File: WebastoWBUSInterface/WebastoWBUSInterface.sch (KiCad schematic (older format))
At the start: 14 parts, among them J1 FTDI Interface, J2 WBUS, Q1 BC548, Q2 BC548, Q3 BC548, Q4 BC557

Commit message: Larger resistor hole sizes
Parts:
- J2: footprint Socket_Strips:Socket_Strip_Angled_1x03_Pitch2.54mm -> Connectors_Terminal_Blocks:TerminalBlock_bornier-3_P5.08mm
- R1, R10, R3, R5, R7, R8, R9: footprint Resistors_THT:R_Axial_DIN0204_L3.6mm_D1.6mm_P5.08mm_Horizontal -> Resistors_THT:R_Axial_DIN0207_L6.3mm_D2.5mm_P7.62mm_Horizontal
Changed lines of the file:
@@
 EESchema Schematic File Version 4
+LIBS:WebastoWBUSInterface-cache
 EELAYER 29 0
 EELAYER END
@@
 F 1 "BC548" H 2400 3540 50  0000 L CNN
 F 2 "TO_SOT_Packages_THT:TO-92_Molded_Narrow" H 2780 3305 50  0001 L CIN
-F 3 "http://www.fairchildsemi.com/ds/BC/BC547.pdf" H 2580 3380 50  0001 L CNN
+F 3 "https://en.wikipedia.org/wiki/BC548" H 2580 3380 50  0001 L CNN
 	1    2580 3380
 	1    0    0    -1
@@
 F 0 "R7" H 3260 3256 50  0000 L CNN
 F 1 "10K" H 3260 3165 50  0000 L CNN
-F 2 "Resistors_THT:R_Axial_DIN0204_L3.6mm_D1.6mm_P5.08mm_Horizontal" V 3120 3210 50  0001 C CNN
+F 2 "Resistors_THT:R_Axial_DIN0207_L6.3mm_D2.5mm_P7.62mm_Horizontal" V 3120 3210 50  0001 C CNN
 F 3 "~" H 3190 3210 50  0001 C CNN
 	1    3190 3210
@@
 F 1 "BC557" H 4461 3115 50  0000 L CNN
 F 2 "TO_SOT_Packages_THT:TO-92_Molded_Narrow" H 4470 2995 50  0001 L CIN
-F 3 "http://www.fairchildsemi.com/ds/BC/BC557.pdf" H 4270 3070 50  0001 L CNN
+F 3 "http://www.farnell.com/datasheets/296678.pdf" H 4270 3070 50  0001 L CNN
 	1    4270 3070
 	-1   0    0    1
@@
 F 0 "R9" H 3570 3186 50  0000 L CNN
 F 1 "1K" H 3570 3095 50  0000 L CNN
-F 2 "Resistors_THT:R_Axial_DIN0204_L3.6mm_D1.6mm_P5.08mm_Horizontal" V 3430 3140 50  0001 C CNN
+F 2 "Resistors_THT:R_Axial_DIN0207_L6.3mm_D2.5mm_P7.62mm_Horizontal" V 3430 3140 50  0001 C CNN
 F 3 "~" H 3500 3140 50  0001 C CNN
 	1    3500 3140
@@
 F 0 "R5" H 3570 3616 50  0000 L CNN
 F 1 "1K" H 3570 3525 50  0000 L CNN
-F 2 "Resistors_THT:R_Axial_DIN0204_L3.6mm_D1.6mm_P5.08mm_Horizontal" V 3430 3570 50  0001 C CNN
+F 2 "Resistors_THT:R_Axial_DIN0207_L6.3mm_D2.5mm_P7.62mm_Horizontal" V 3430 3570 50  0001 C CNN
 F 3 "~" H 3500 3570 50  0001 C CNN
 	1    3500 3570
@@
 F 0 "J2" H 5788 3306 50  0000 L CNN
 F 1 "WBUS" H 5788 3215 50  0000 L CNN
-F 2 "Socket_Strips:Socket_Strip_Angled_1x03_Pitch2.54mm" H 5760 3280 50  0001 C CNN
+F 2 "Connectors_Terminal_Blocks:TerminalBlock_bornier-3_P5.08mm" H 5760 3280 50  0001 C CNN
 F 3 "~" H 5760 3280 50  0001 C CNN
 	1    5760 3280
@@
 F 0 "R10" V 4413 3380 50  0000 C CNN
 F 1 "10K" V 4504 3380 50  0000 C CNN
-F 2 "Resistors_THT:R_Axial_DIN0204_L3.6mm_D1.6mm_P5.08mm_Horizontal" V 4550 3380 50  0001 C CNN
+F 2 "Resistors_THT:R_Axial_DIN0207_L6.3mm_D2.5mm_P7.62mm_Horizontal" V 4550 3380 50  0001 C CNN
 F 3 "~" H 4620 3380 50  0001 C CNN
 	1    4620 3380
@@
 F 0 "R3" H 4840 3024 50  0000 R CNN
 F 1 "1K" H 4840 3115 50  0000 R CNN
-F 2 "Resistors_THT:R_Axial_DIN0204_L3.6mm_D1.6mm_P5.08mm_Horizontal" V 4840 3070 50  0001 C CNN
+F 2 "Resistors_THT:R_Axial_DIN0207_L6.3mm_D2.5mm_P7.62mm_Horizontal" V 4840 3070 50  0001 C CNN
 F 3 "~" H 4910 3070 50  0001 C CNN
 	1    4910 3070
@@
 F 0 "R8" H 3120 3844 50  0000 R CNN
 F 1 "10K" H 3120 3935 50  0000 R CNN
-F 2 "Resistors_THT:R_Axial_DIN0204_L3.6mm_D1.6mm_P5.08mm_Horizontal" V 3120 3890 50  0001 C CNN
+F 2 "Resistors_THT:R_Axial_DIN0207_L6.3mm_D2.5mm_P7.62mm_Horizontal" V 3120 3890 50  0001 C CNN
 F 3 "~" H 3190 3890 50  0001 C CNN
 	1    3190 3890
@@
 F 1 "BC548" H 4431 4655 50  0000 L CNN
 F 2 "TO_SOT_Packages_THT:TO-92_Molded_Narrow" H 4440 4625 50  0001 L CIN
-F 3 "http://www.fairchildsemi.com/ds/BC/BC547.pdf" H 4240 4700 50  0001 L CNN
+F 3 "https://en.wikipedia.org/wiki/BC548" H 4240 4700 50  0001 L CNN
 	1    4240 4700
 	1    0    0    -1
@@
 F 0 "R1" V 4473 4500 50  0000 C CNN
 F 1 "10K" V 4564 4500 50  0000 C CNN
-F 2 "Resistors_THT:R_Axial_DIN0204_L3.6mm_D1.6mm_P5.08mm_Horizontal" V 4610 4500 50  0001 C CNN
+F 2 "Resistors_THT:R_Axial_DIN0207_L6.3mm_D2.5mm_P7.62mm_Horizontal" V 4610 4500 50  0001 C CNN
 F 3 "~" H 4680 4500 50  0001 C CNN
 	1    4680 4500
@@
 F 1 "BC548" H 5281 4455 50  0000 L CNN
 F 2 "TO_SOT_Packages_THT:TO-92_Molded_Narrow" H 5290 4425 50  0001 L CIN
-F 3 "http://www.fairchildsemi.com/ds/BC/BC547.pdf" H 5090 4500 50  0001 L CNN
+F 3 "https://en.wikipedia.org/wiki/BC548" H 5090 4500 50  0001 L CNN
 	1    5090 4500
 	1    0    0    -1

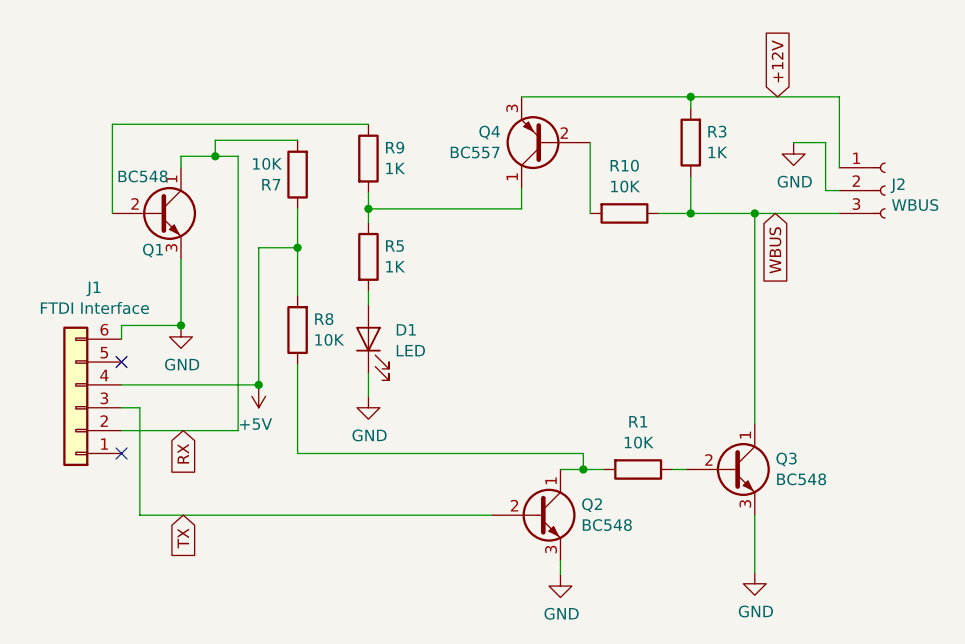
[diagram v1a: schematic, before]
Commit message: JLCPCB SMD board for full assembly
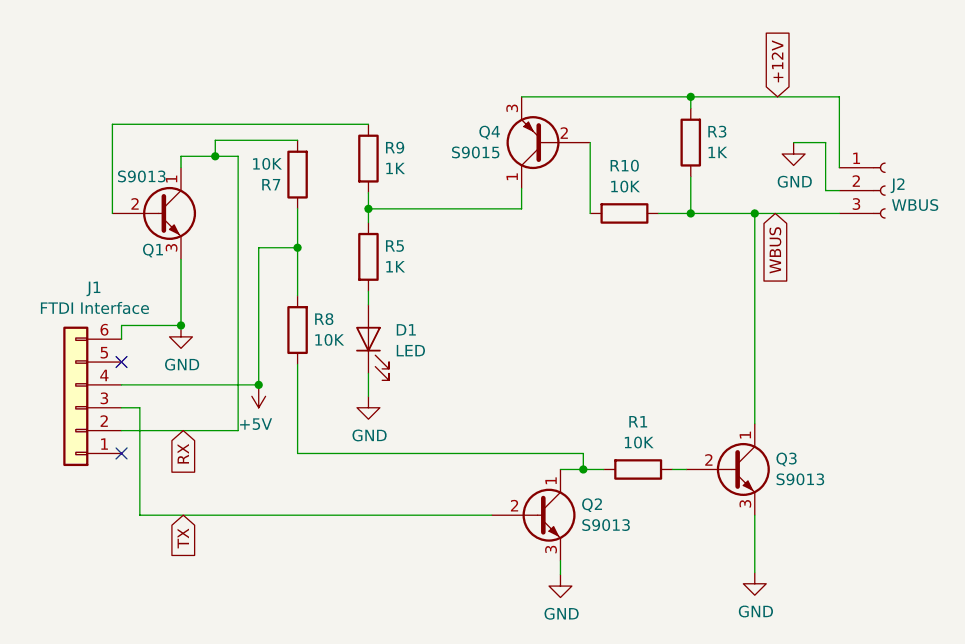
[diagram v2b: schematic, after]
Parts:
- D1: footprint LEDs:LED_D3.0mm -> LEDs:LED_0603_HandSoldering; JLCPCBPartNumber (none) -> C72043
- Q1, Q2, Q3: value BC548 -> S9013; footprint TO_SOT_Packages_THT:TO-92_Molded_Narrow -> TO_SOT_Packages_SMD:SOT-23; JLCPCBPartNumber (none) -> C6749; Part (none) -> S9013
- Q4: value BC557 -> S9015; footprint TO_SOT_Packages_THT:TO-92_Molded_Narrow -> TO_SOT_Packages_SMD:SOT-23; JLCPCBPartNumber (none) -> C2149; Part (none) -> S9015
- R1, R10, R7, R8: footprint Resistors_THT:R_Axial_DIN0207_L6.3mm_D2.5mm_P7.62mm_Horizontal -> Resistors_SMD:R_0805_HandSoldering; JLCPCBPartNumber (none) -> C17414; Part (none) -> 0805W8F1002T5E
- R3, R5, R9: footprint Resistors_THT:R_Axial_DIN0207_L6.3mm_D2.5mm_P7.62mm_Horizontal -> Resistors_SMD:R_0805_HandSoldering; JLCPCBPartNumber (none) -> C17513; Part (none) -> 0805W8F1001T5E
